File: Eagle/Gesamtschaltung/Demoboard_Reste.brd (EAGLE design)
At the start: 106.7 x 149.9 mm, 105 parts, among them IC04 24LC256, IC06 LM1117-5.0, IC1 MC9S08AW60, Q1 4M9152, X4 SPP

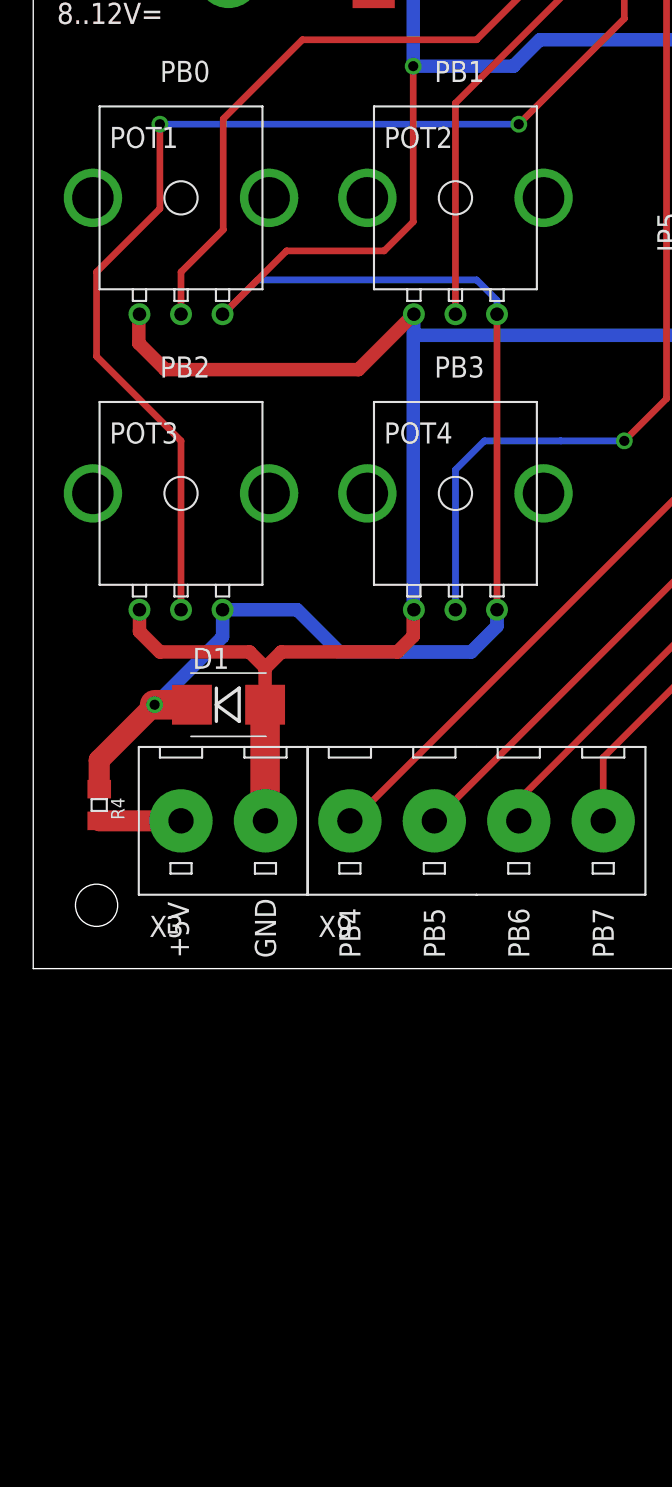
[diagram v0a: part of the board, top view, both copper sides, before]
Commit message: exp Dokumentation, 9 pages now
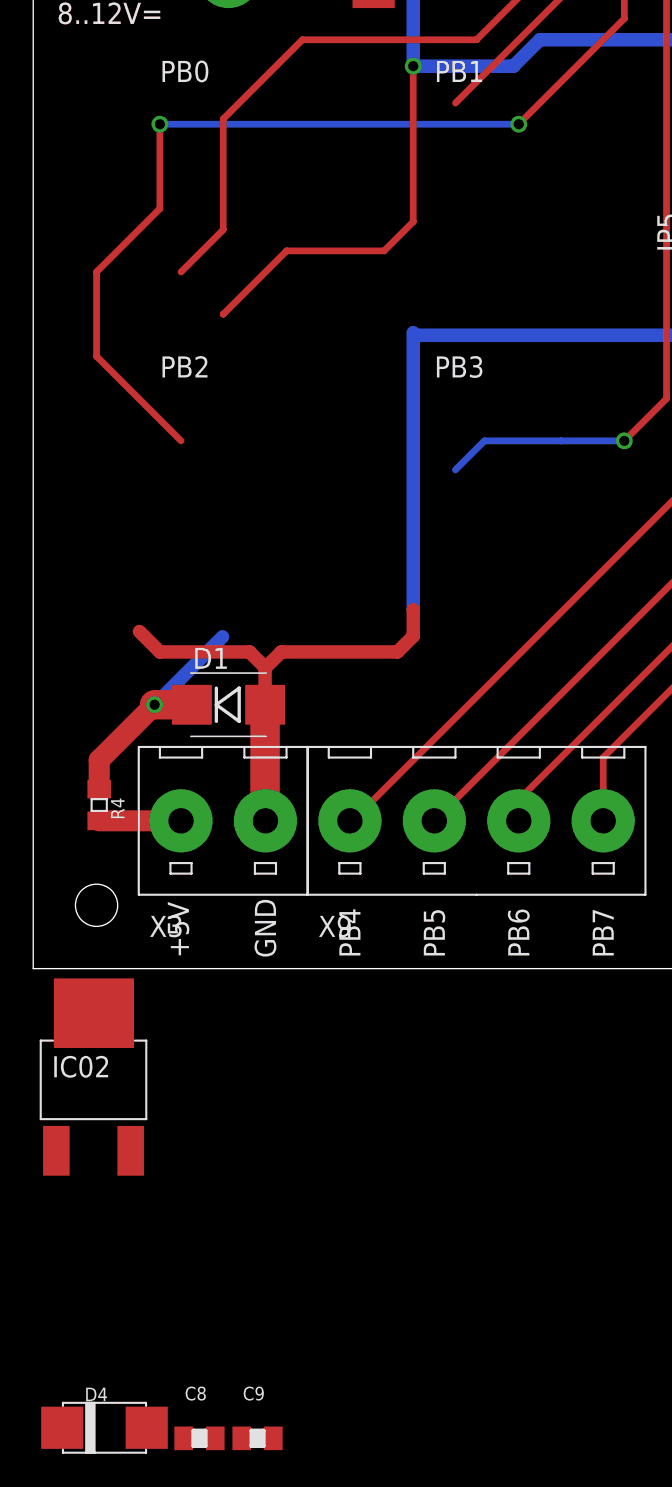
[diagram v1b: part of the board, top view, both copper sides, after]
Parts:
- removed POT1, POT2, POT3, POT4: 50k, pot:ALPS_VERTICAL
- added C8, C9: 1µF, deto:0805F
- added D4: 1N4007, deto:MELF_B
- added IC02: LM1117-5.0, deto:DPAK
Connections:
- new net N$1: C8.2, D4.K, IC02.3
- net +5V: now also C9.2, IC02.4; no longer POT1.3, POT2.3, POT3.3, POT4.3
- net ANA0: no longer POT1.2
- net ANA1: no longer POT2.2
- net ANA2: no longer POT3.2
- net ANA3: no longer POT4.2
- net GND: now also C8.1, C9.1, IC02.1; no longer POT1.1, POT2.1, POT3.1, POT4.1
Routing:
- net +5V: track 568.5 -> 511.1 mm
- net GND: track 653.3 -> 630.4 mm
- net ANA1: track 23.8 -> 11.1 mm
- net ANA2: track 66.3 -> 56.2 mm
- net ANA3: track 48.6 -> 40.2 mm
- net ANA0: track 35.7 -> 33.2 mm
